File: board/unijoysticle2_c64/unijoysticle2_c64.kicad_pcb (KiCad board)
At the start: 4 copper layers, 62.5 x 60 mm, 62 parts, among them J1 USB_B_Micro, J2 PORT JOY #1, J3 PORT JOY #2, Q1 S8050, Q2 S8050, SW1 RESET, SW2 BOOT, SW3 MODE, SW4 SWAP, U1 ESP32-WROOM-32E, U2 AMS1117-3.3, U3 CH340C, U4 74HC05, U5 74HC05, U6 74HC05

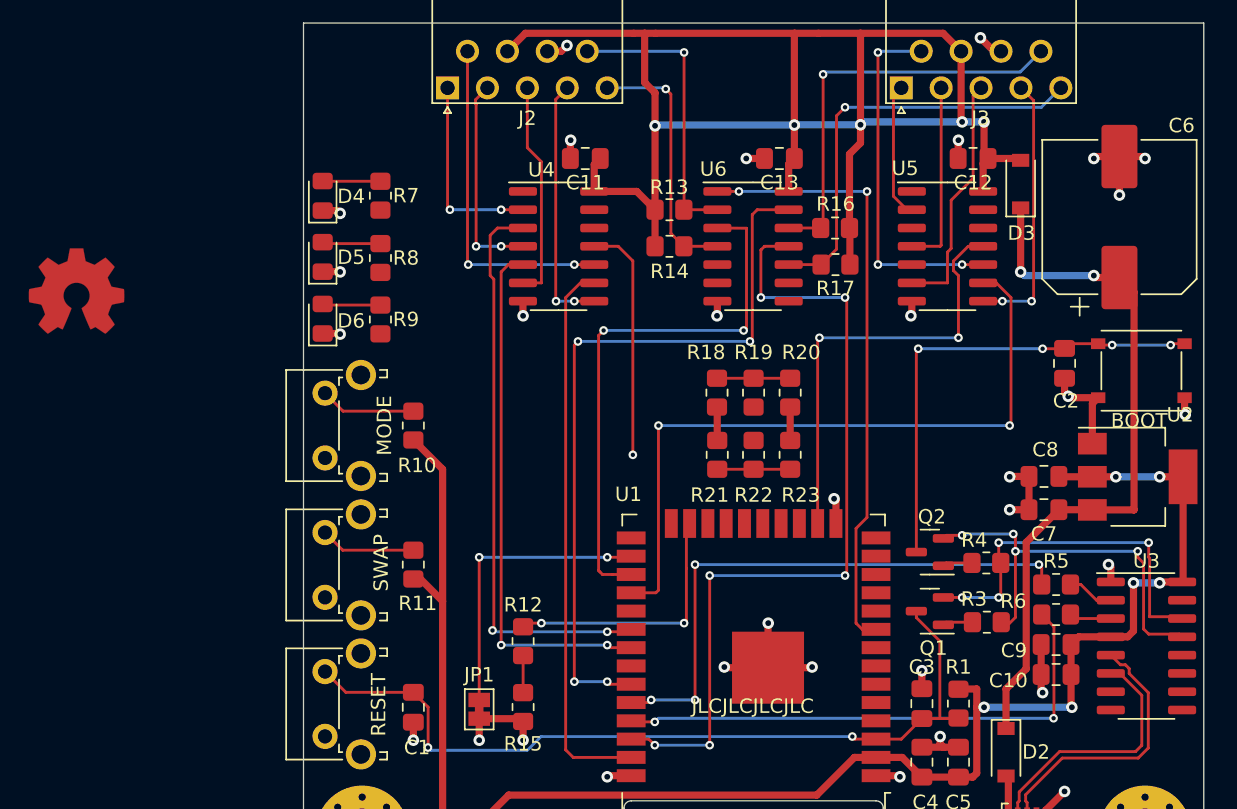
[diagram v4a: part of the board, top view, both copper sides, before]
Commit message: c64: routing finished...
...but requires more polishing
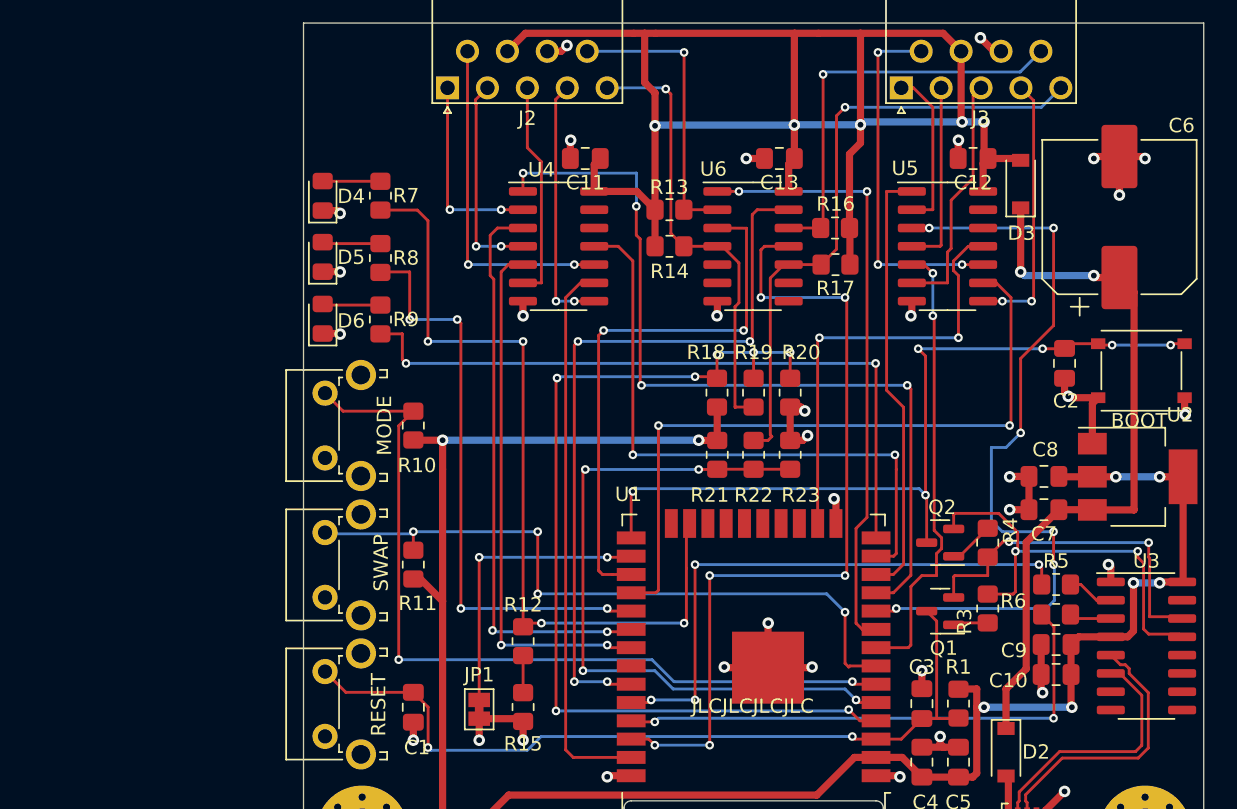
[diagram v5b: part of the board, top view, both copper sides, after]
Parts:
- removed REF**: OSHW-Symbol_6.7x6mm_Copper, Symbol:OSHW-Symbol_6.7x6mm_Copper
- moved R4 1.41 mm to (129.8, 126.1), turned to -90 degrees
- moved Q2 0.97 mm to (126.5, 126.1)
- moved R3 0.95 mm to (129.8, 130.6), turned to 90 degrees
- moved Q1 0.72 mm to (126.5, 130.8)
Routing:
- net GPIO_36: track 5.08 -> 67.4 mm, vias 0 -> 7
- net GPIO_J1_UP: track 0.00 -> 58.8 mm, vias 0 -> 4
- net GPIO_J2_DOWN: track 0.00 -> 54.7 mm, vias 0 -> 6
- net GPIO_SWITCH_USER1: track 6.65 -> 58.2 mm, vias 0 -> 2
- net GPIO_LED_J2: track 0.00 -> 48.4 mm, vias 0 -> 2
- net GPIO_39: track 5.06 -> 49.5 mm, vias 0 -> 4
- net GPIO_SWITCH_USER2: track 6.64 -> 48.2 mm, vias 0 -> 4
- net GPIO_LED_J1: track 0.00 -> 40.7 mm, vias 0 -> 4
- net GPIO_BOOTSTRAP_15_LED_BT: track 18.4 -> 56.8 mm, vias 2 -> 4
- net GPIO_J2_LEFT: track 0.00 -> 31.7 mm, vias 0 -> 2
- net GPIO_J2_UP: track 0.00 -> 30.3 mm
- net GPIO_J1_FIRE: track 16.6 -> 43.1 mm, vias 1 -> 2
- net /ESP32/ESP_BOOT: track 32.9 -> 56.5 mm, vias 4 -> 6
- net +3V3: track 118.1 -> 138.3 mm, vias 6 -> 8
- net /C64 Ports/J2_POTY: track 29.4 -> 43.5 mm
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
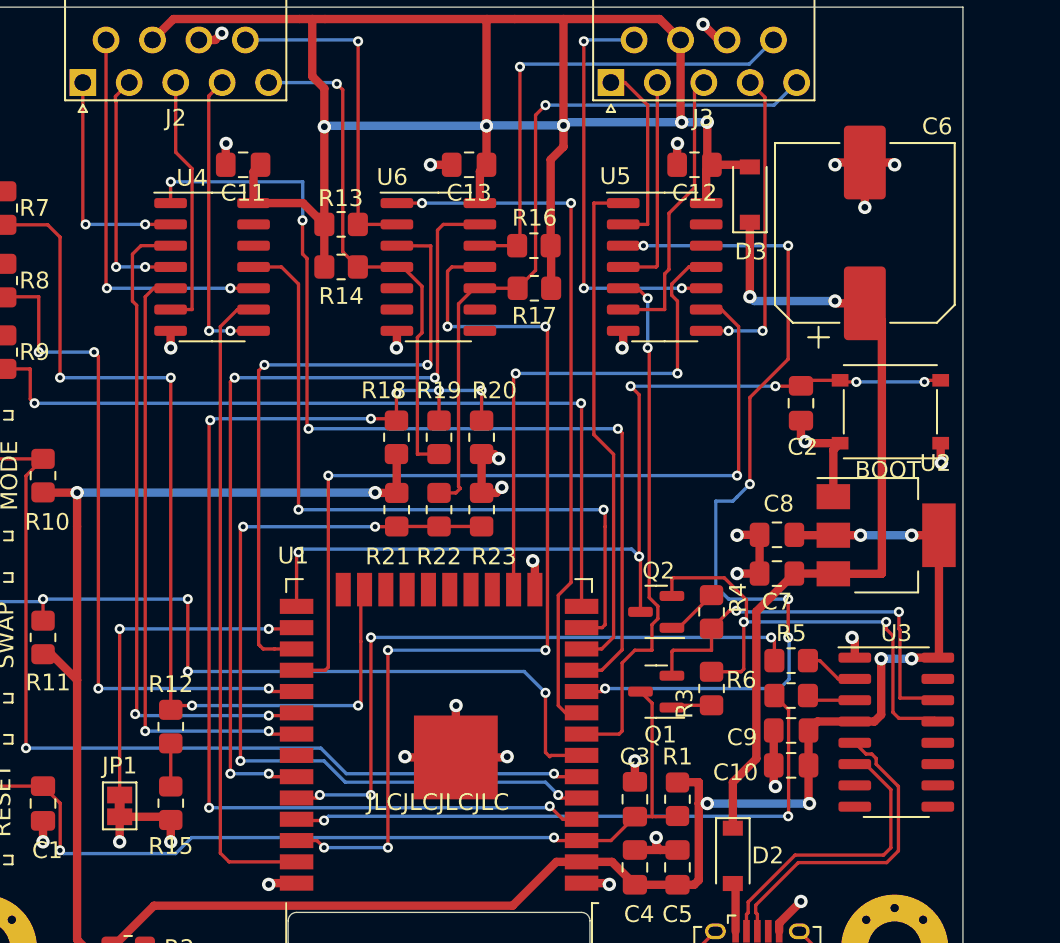
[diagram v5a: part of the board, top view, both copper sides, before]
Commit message: c64: routing/layout improvements
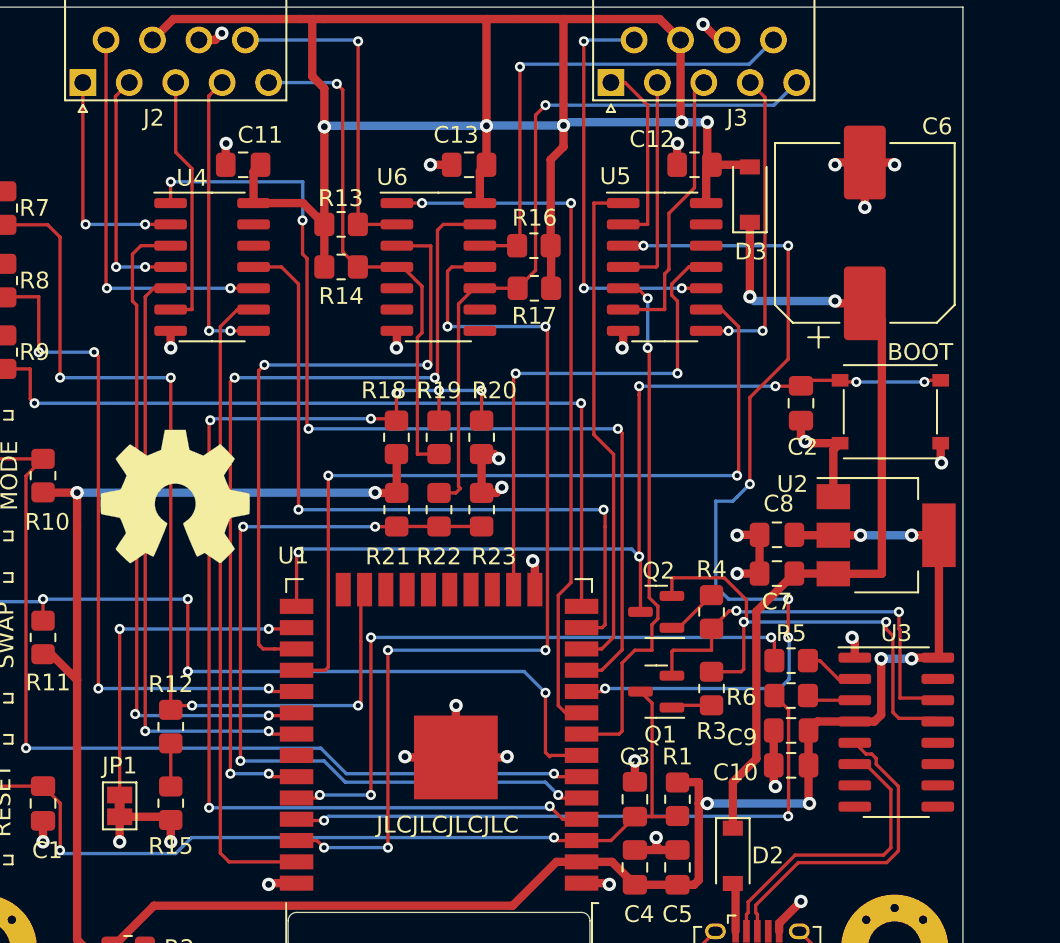
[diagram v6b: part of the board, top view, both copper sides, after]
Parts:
- added REF**: OSHW-Symbol_8.9x8mm_SilkScreen, Symbol:OSHW-Symbol_8.9x8mm_SilkScreen, F.Cu at (97.7, 119.2)
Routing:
- net /ESP32/ESP_BOOT: track 56.5 -> 55.6 mm
- net GND: track 73.4 -> 72.9 mm
